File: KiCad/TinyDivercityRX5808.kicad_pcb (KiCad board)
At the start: 2 copper layers, 22 x 19.7 mm, 31 parts, among them J1 Googles, J2 RX_A, J3 RX_B, J4 Conn_01x06, SW1 SW_Push, U1 MAX4624, U2 ATTINY85-20SU

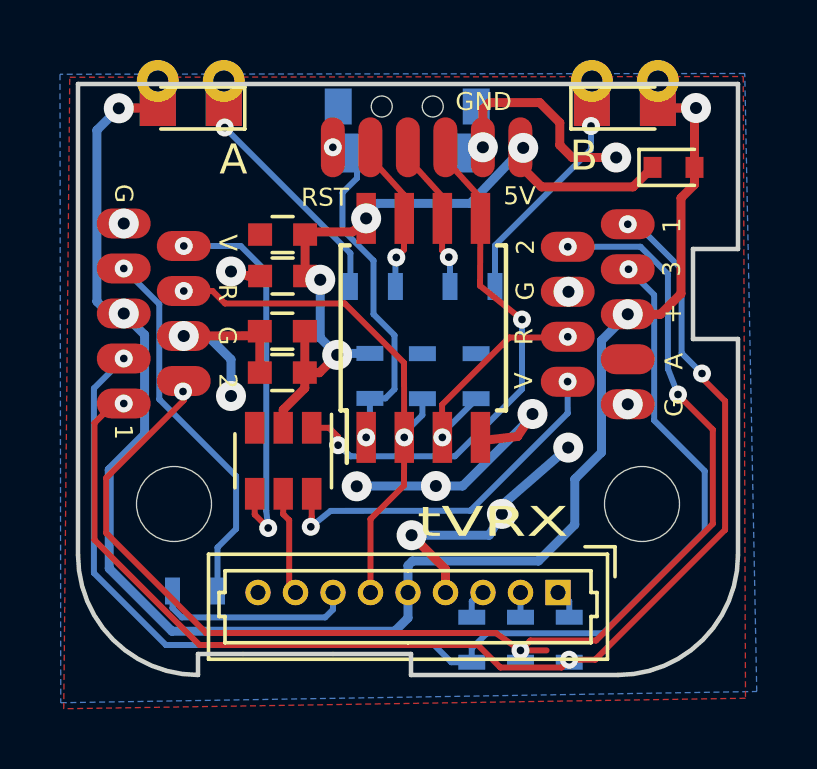
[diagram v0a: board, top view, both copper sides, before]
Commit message: Changed via drill size to 0.3mm
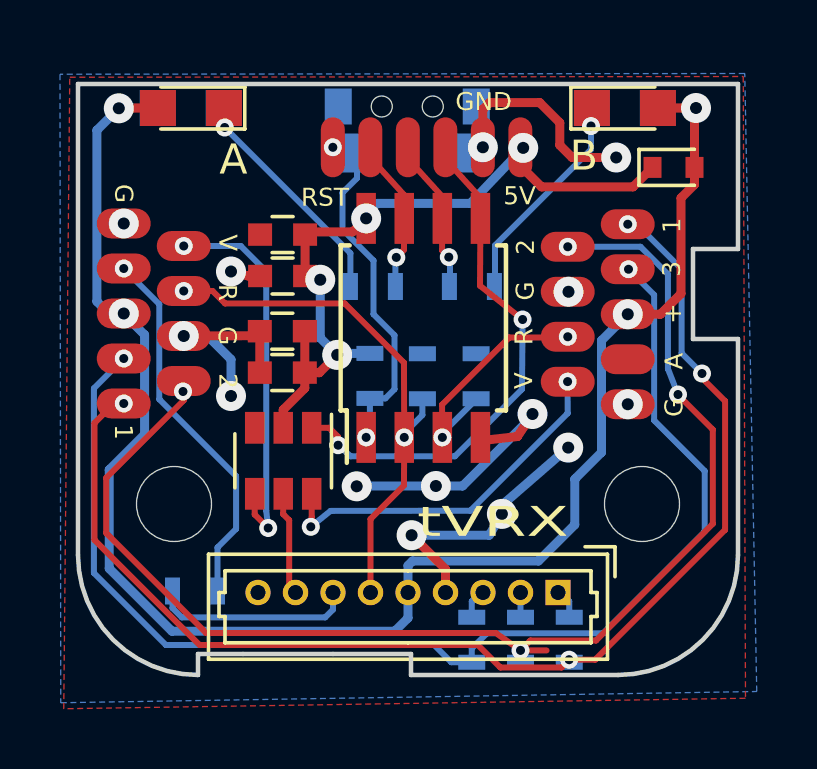
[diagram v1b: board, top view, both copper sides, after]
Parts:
- removed the REF** at (131.5, 91.8)
- removed the REF** at (133.7, 92.0)
- removed the REF** at (145.9, 92.0)
- removed the REF** at (148.1, 92.0)
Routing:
- net VCC: track 59.3 -> 57.5 mm
- net Net-(D2-Pad1): track 8.79 -> 7.89 mm
- net Net-(D1-Pad1): track 9.88 -> 8.98 mm
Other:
- net class Default: via_drill 0.254 -> 0.3
- rule via_min_drill: 0.254 -> 0.3

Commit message: Moved 30 ohm resistor
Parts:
- moved R8 13.4 mm to (132.1, 95.5), turned to 180 degrees
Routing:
- net /AUD_IN: track 6.73 -> 19.8 mm
- net /AUD_OUT: track 12.6 -> 3.07 mm
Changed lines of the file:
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@@
     (thickness 0.8)
     (drawings 55)
-    (tracks 316)
+    (tracks 319)
     (zones 0)
     (modules 27)
@@
   )
   (module Resistors_SMD:R_0603 (layer B.Cu)
-    (at 132.7 108.95)
+    (at 132.1 95.55 180)
     (descr "Resistor SMD 0603, reflow soldering, Vishay (see dcrcw.pdf)")
     (tags "resistor 0603")
     (attr smd)
-    (fp_text reference R8 (at 0 1.45) (layer B.SilkS) hide
-      (effects (font (size 1 1) (thickness 0.15)) (justify mirror))
-    )
-    (fp_text value 30 (at 0 -1.5) (layer B.Fab) hide
-      (effects (font (size 1 1) (thickness 0.15)) (justify mirror))
-    )
-    (fp_text user %R (at 0 0) (layer B.Fab)
+    (fp_text reference R8 (at 0 1.45 180) (layer B.SilkS) hide
+      (effects (font (size 1 1) (thickness 0.15)) (justify mirror))
+    )
+    (fp_text value 30 (at 0 -1.5 180) (layer B.Fab) hide
+      (effects (font (size 1 1) (thickness 0.15)) (justify mirror))
+    )
+    (fp_text user %R (at 0 0 180) (layer B.Fab)
       (effects (font (size 0.4 0.4) (thickness 0.075)) (justify mirror))
     )
@@
     (fp_line (start 1.25 -0.7) (end 1.25 0.7) (layer B.CrtYd) (width 0.05))
     (fp_line (start 1.25 -0.7) (end -1.25 -0.7) (layer B.CrtYd) (width 0.05))
-    (pad 1 smd rect (at -0.75 0) (size 0.5 0.9) (layers B.Cu B.Paste B.Mask)
+    (pad 1 smd rect (at -0.75 0 180) (size 0.5 0.9) (layers B.Cu B.Paste B.Mask)
       (net 10 /AUD_IN))
-    (pad 2 smd rect (at 0.75 0) (size 0.5 0.9) (layers B.Cu B.Paste B.Mask)
+    (pad 2 smd rect (at 0.75 0 180) (size 0.5 0.9) (layers B.Cu B.Paste B.Mask)
       (net 15 /AUD_OUT))
     (model ${KISYS3DMOD}/Resistors_SMD.3dshapes/R_0603.wrl
@@
     (effects (font (size 0.7 0.7) (thickness 0.15)) (justify mirror))
   )
-  (gr_text 30 (at 130.49 108.99) (layer B.SilkS)
+  (gr_text 30 (at 134.16 95.51) (layer B.SilkS)
     (effects (font (size 0.7 0.7) (thickness 0.15)) (justify mirror))
   )
@@
   (segment (start 140.28 102.54) (end 140.28 103.085) (width 0.2) (layer B.Cu) (net 9))
   (segment (start 140.28 103.085) (end 139.665 103.7) (width 0.2) (layer B.Cu) (net 9))
-  (segment (start 131.95 108.95) (end 131.95 109.52) (width 0.2) (layer B.Cu) (net 10))
-  (segment (start 137.3 109.57) (end 137.3 109) (width 0.2) (layer B.Cu) (net 10))
-  (segment (start 137.04 109.83) (end 137.3 109.57) (width 0.2) (layer B.Cu) (net 10))
-  (segment (start 132.26 109.83) (end 137.04 109.83) (width 0.2) (layer B.Cu) (net 10))
-  (segment (start 131.95 109.52) (end 132.26 109.83) (width 0.2) (layer B.Cu) (net 10))
+  (segment (start 132.85 95.55) (end 132.85 95.89) (width 0.2) (layer B.Cu) (net 10) (status C00000))
+  (segment (start 132.85 95.89) (end 131.65 97.09) (width 0.2) (layer B.Cu) (net 10) (status 400000))
+  (segment (start 131.65 97.09) (end 131.65 99.61) (width 0.2) (layer B.Cu) (net 10))
+  (segment (start 131.65 99.61) (end 131.46 99.8) (width 0.2) (layer B.Cu) (net 10))
+  (segment (start 131.46 99.8) (end 131.46 102.31) (width 0.2) (layer B.Cu) (net 10))
+  (segment (start 131.46 102.31) (end 134.09 104.94) (width 0.2) (layer B.Cu) (net 10))
+  (segment (start 134.09 104.94) (end 134.09 107.68) (width 0.2) (layer B.Cu) (net 10))
+  (segment (start 134.09 107.68) (end 133.59 108.18) (width 0.2) (layer B.Cu) (net 10))
+  (segment (start 133.59 108.18) (end 133.59 109.24) (width 0.2) (layer B.Cu) (net 10))
+  (segment (start 133.59 109.24) (end 134.09 109.74) (width 0.2) (layer B.Cu) (net 10))
+  (segment (start 134.09 109.74) (end 136.56 109.74) (width 0.2) (layer B.Cu) (net 10))
+  (segment (start 136.56 109.74) (end 137.3 109) (width 0.2) (layer B.Cu) (net 10) (status 800000))
   (segment (start 135.64 105.71) (end 135.64 106.39) (width 0.2) (layer F.Cu) (net 11))
   (segment (start 135.84 106.59) (end 135.84 108.79) (width 0.2) (layer F.Cu) (net 11))
@@
   (segment (start 129.33 102.195) (end 129.33 108.35) (width 0.2) (layer B.Cu) (net 14))
   (segment (start 129.33 102.195) (end 130.325 101.2) (width 0.2) (layer B.Cu) (net 14))
-  (segment (start 134.07 106.88) (end 133.45 107.5) (width 0.2) (layer B.Cu) (net 15))
-  (segment (start 130.325 98.2) (end 130.32 98.2) (width 0.2) (layer B.Cu) (net 15))
-  (segment (start 130.32 98.2) (end 131.51 99.39) (width 0.2) (layer B.Cu) (net 15))
-  (segment (start 131.51 99.39) (end 131.51 102.56) (width 0.2) (layer B.Cu) (net 15))
-  (segment (start 131.51 102.56) (end 134.07 105.12) (width 0.2) (layer B.Cu) (net 15))
-  (segment (start 134.07 105.12) (end 134.07 106.88) (width 0.2) (layer B.Cu) (net 15))
-  (via (at 130.325 98.2) (size 0.6) (drill 0.3) (layers F.Cu B.Cu) (net 15))
-  (segment (start 133.45 107.5) (end 133.45 108.95) (width 0.2) (layer B.Cu) (net 15))
+  (via (at 130.325 98.2) (size 0.6) (drill 0.3) (layers F.Cu B.Cu) (net 15) (status C00000))
+  (segment (start 131.15 95.75) (end 131.15 97.375) (width 0.2) (layer B.Cu) (net 15) (status 400000))
+  (segment (start 131.15 97.375) (end 130.325 98.2) (width 0.2) (layer B.Cu) (net 15) (status 800000))
+  (segment (start 131.15 95.75) (end 131.35 95.55) (width 0.2) (layer B.Cu) (net 15) (status C00000))
   (segment (start 134.69 105.71) (end 134.69 106.4) (width 0.2) (layer F.Cu) (net 16))
   (segment (start 134.69 106.4) (end 135.14 106.85) (width 0.2) (layer F.Cu) (net 16))
